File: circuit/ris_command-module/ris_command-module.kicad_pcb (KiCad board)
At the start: 2 copper layers, 48 x 71 mm, 7 parts, among them J1 JST-PH-5P-M, J3 JST-PH-2P-M, SW3 SW_DIP_x01, U1 AM2302_DHT22, U6 ESP32-DEVKITC-32D

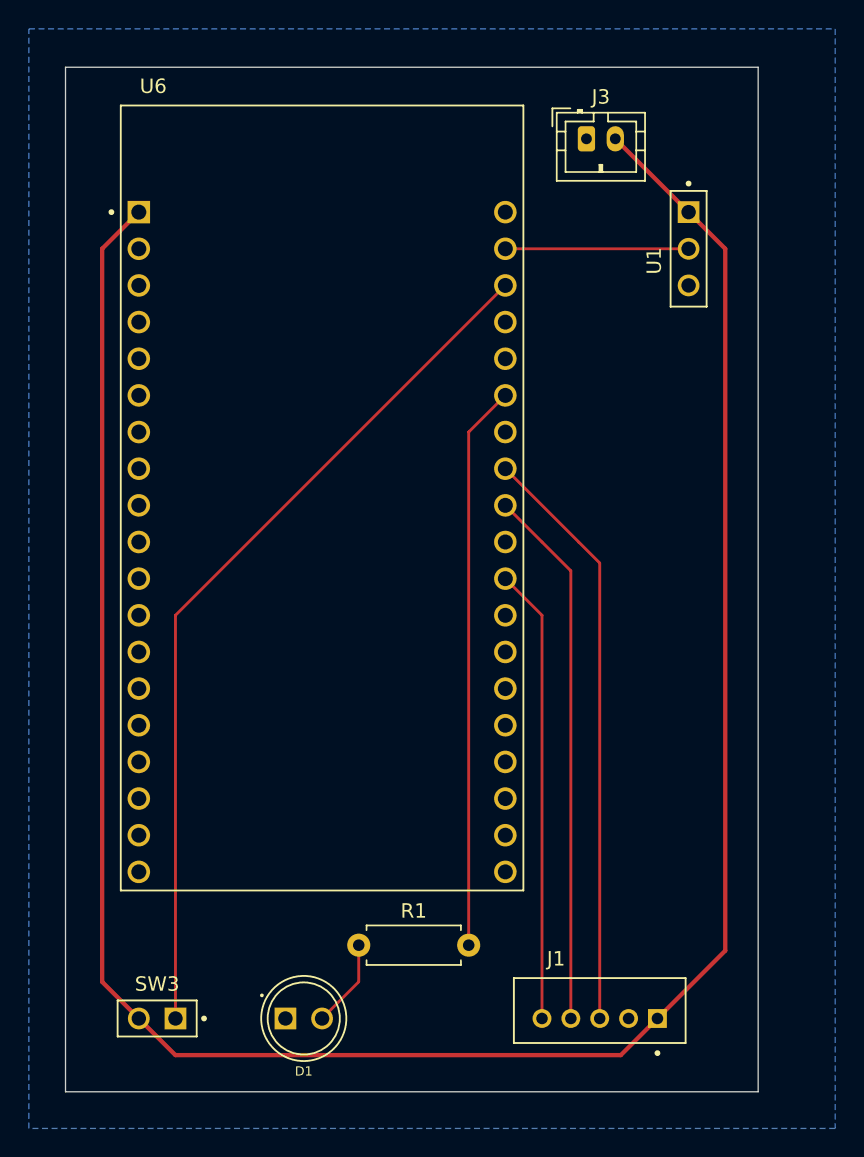
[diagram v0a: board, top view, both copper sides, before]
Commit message: Updated Circuit with Side Outputs & Mosfets
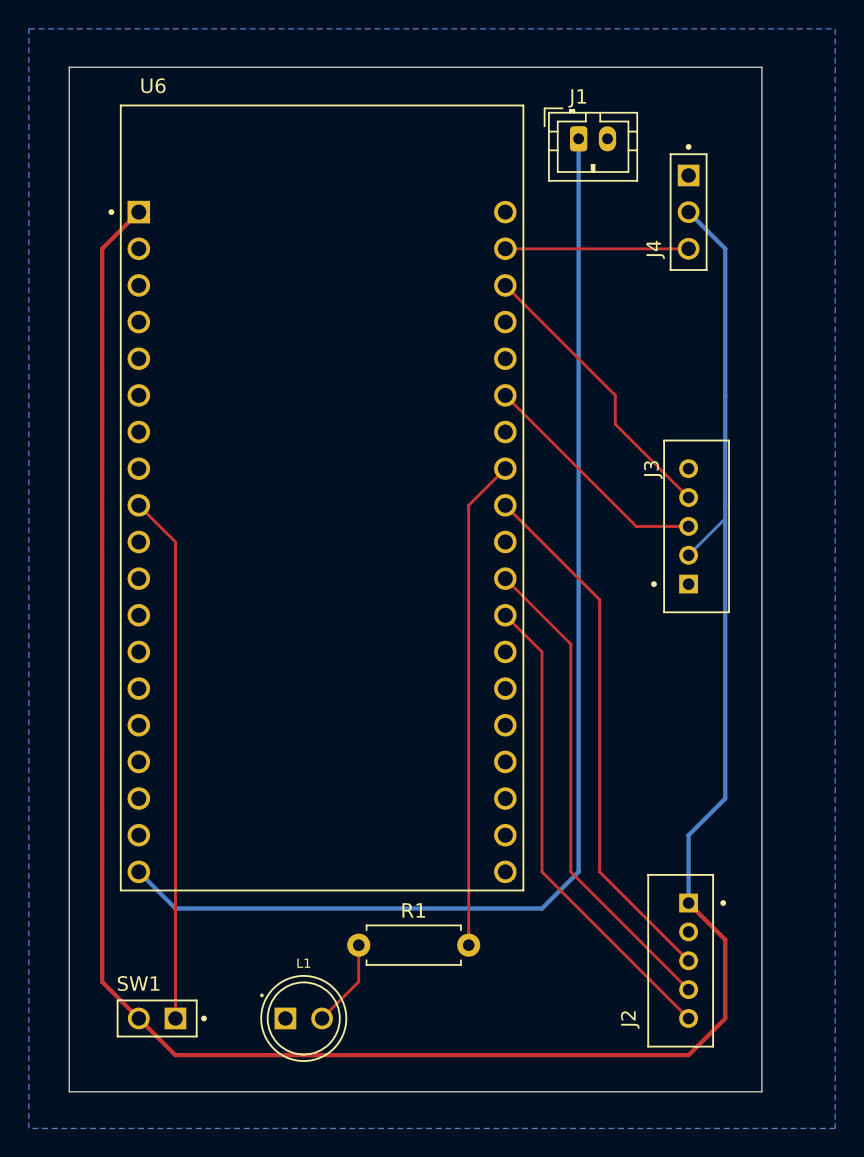
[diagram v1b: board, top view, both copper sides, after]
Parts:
- removed SW3: SW_DIP_x01, socket-headers-2pin:HARWIN_M20-7820242
- removed U1: AM2302_DHT22, socket-headers-3pin:HARWIN_M20-7820346
- added J1: JST-PH-2P-M_5V, Connector_JST:JST_PH_B2B-PH-K_1x02_P2.00mm_Vertical, F.Cu at (160.0, 68.6)
- added J4: Header-3P-F_DHT22, socket-headers-3pin:HARWIN_M20-7820346, F.Cu at (167.6, 73.7)
- added SW1: SW_DIP_x01, socket-headers-2pin:HARWIN_M20-7820242, F.Cu at (132.1, 129.5)
- J3: value JST-PH-2P-M -> JST-PH-5P-M_ZS042; footprint Connector_JST:JST_PH_B2B-PH-K_1x02_P2.00mm_Vertical -> B5B-PH-K-S:JST_B5B-PH-K-S
- moved J3 27.9 mm to (168.2, 95.4), turned to -90 degrees
- moved J2 6.59 mm to (167.1, 125.5), turned to 90 degrees
- renumbered J1 to J2, D1 to L1
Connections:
- J2 pad 3: Net-(J1-Pin_3) -> Net-(J2-Pin_3)
- J2 pad 4: Net-(J1-Pin_4) -> Net-(J2-Pin_4)
- J2 pad 5: Net-(J1-Pin_5) -> Net-(J2-Pin_5)
- R1 pad 2: Net-(U6-IO21) -> Net-(U6-IO19)
- U6 pad J2-19: unconnected-(U6-EXT_5V-PadJ2-19) -> +5V
- U6 pad J2-9: unconnected-(U6-IO25-PadJ2-9) -> Net-(U6-IO25)
- U6 pad J3-11: Net-(J1-Pin_5) -> Net-(J2-Pin_4)
- U6 pad J3-12: unconnected-(U6-IO16-PadJ3-12) -> Net-(J2-Pin_5)
- U6 pad J3-3: Net-(U6-IO22) -> Net-(J3-Pin_4)
- U6 pad J3-6: Net-(U6-IO21) -> Net-(J3-Pin_3)
- U6 pad J3-8: Net-(J1-Pin_3) -> Net-(U6-IO19)
- U6 pad J3-9: Net-(J1-Pin_4) -> Net-(J2-Pin_3)
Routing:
- net +5V: track 0.00 -> 83.4 mm
- net Net-(U6-IO22): track 60.3 -> 0.00 mm
- net Net-(J1-Pin_3): track 40.8 -> 0.00 mm
- net Net-(U6-IO21): track 39.2 -> 0.00 mm
- net Net-(J1-Pin_4): track 37.4 -> 0.00 mm
- net Net-(J2-Pin_3): track 0.00 -> 36.8 mm
- net Net-(U6-IO25): track 0.00 -> 36.6 mm
- net Net-(U6-IO19): track 0.00 -> 34.1 mm
- net Net-(J2-Pin_4): track 0.00 -> 33.7 mm
- net Net-(J2-Pin_5): track 0.00 -> 33.2 mm
- net Net-(J1-Pin_5): track 31.5 -> 0.00 mm
- net Net-(J3-Pin_4): track 0.00 -> 20.0 mm
- net Net-(J3-Pin_3): track 0.00 -> 16.8 mm
- net +3.3V: track 162.1 -> 164.3 mm

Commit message: Updated Model with Connectors / Slots
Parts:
- moved J2 4.70 mm to (167.1, 120.8)
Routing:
- net Net-(J2-Pin_3): track 36.8 -> 32.5 mm
- net Net-(J2-Pin_4): track 33.7 -> 29.4 mm
- net Net-(J2-Pin_5): track 33.2 -> 28.9 mm
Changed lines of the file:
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@@
 	(footprint "B5B-PH-K-S:JST_B5B-PH-K-S"
 		(layer "F.Cu")
-		(at 167.09 125.54 90)
+		(at 167.09 120.84 90)
 		(property "Reference" "J2"
 			(at -4 -3.585 90)
@@
 		(model "G:/projects/primary/regulated-irrigation-system/model/asm/electronic-components/jst-ph-5p_short/jst-ph-5p_short.step"
 			(offset
-				(xyz 4.55 -4.1 6)
+				(xyz 4 -0.55 6)
 			)
 			(scale
@@
 		(model "G:/projects/primary/regulated-irrigation-system/model/asm/electronic-components/led/led.step"
 			(offset
-				(xyz -0.8 -4.5 10.74)
+				(xyz -0.12 -5.68 9.68)
 			)
 			(scale
@@
 		(model "G:/projects/primary/regulated-irrigation-system/model/asm/electronic-components/switch/switch.step"
 			(offset
-				(xyz 5.3 -5.3 13.5)
+				(xyz 9.75 -16.8 18.07)
 			)
 			(scale
@@
 	)
 	(segment
+		(start 170.18 129.54)
+		(end 170.18 119.38)
+		(width 0.3)
+		(layer "F.Cu")
+		(net 3)
+	)
+	(segment
+		(start 129.54 73.66)
+		(end 127 76.2)
+		(width 0.3)
+		(layer "F.Cu")
+		(net 3)
+	)
+	(segment
 		(start 132.08 132.08)
 		(end 167.64 132.08)
@@
 	)
 	(segment
-		(start 129.54 73.66)
-		(end 127 76.2)
+		(start 129.54 129.54)
+		(end 132.08 132.08)
 		(width 0.3)
 		(layer "F.Cu")
@@
 	)
 	(segment
-		(start 170.18 129.54)
-		(end 170.18 124.08)
+		(start 170.18 119.38)
+		(end 167.64 116.84)
 		(width 0.3)
 		(layer "F.Cu")
@@
 	)
 	(segment
-		(start 170.18 124.08)
-		(end 167.64 121.54)
-		(width 0.3)
-		(layer "F.Cu")
-		(net 3)
-	)
-	(segment
 		(start 127 127)
 		(end 129.54 129.54)
-		(width 0.3)
-		(layer "F.Cu")
-		(net 3)
-	)
-	(segment
-		(start 129.54 129.54)
-		(end 132.08 132.08)
 		(width 0.3)
 		(layer "F.Cu")
@@
 	)
 	(segment
-		(start 167.64 121.54)
-		(end 167.64 116.84)
-		(width 0.3)
-		(layer "B.Cu")
-		(net 3)
-	)
-	(segment
 		(start 167.64 97.44)
 		(end 170.18 94.9)
@@
 	)
 	(segment
+		(start 167.02 120.84)
+		(end 161.48 115.3)
+		(width 0.2)
+		(layer "F.Cu")
+		(net 33)
+	)
+	(segment
+		(start 167.64 120.84)
+		(end 167.02 120.84)
+		(width 0.2)
+		(layer "F.Cu")
+		(net 33)
+	)
+	(segment
+		(start 161.48 115.3)
+		(end 161.48 100.52)
+		(width 0.2)
+		(layer "F.Cu")
+		(net 33)
+	)
+	(segment
 		(start 161.48 100.52)
 		(end 154.94 93.98)
@@
 	)
 	(segment
-		(start 167.64 125.54)
-		(end 161.48 119.38)
-		(width 0.2)
-		(layer "F.Cu")
-		(net 33)
-	)
-	(segment
-		(start 161.48 119.38)
-		(end 161.48 100.52)
-		(width 0.2)
-		(layer "F.Cu")
-		(net 33)
-	)
-	(segment
-		(start 167.64 129.54)
-		(end 157.48 119.38)
-		(width 0.2)
-		(layer "F.Cu")
-		(net 34)
-	)
-	(segment
-		(start 157.48 119.38)
-		(end 157.48 104.14)
+		(start 167.02 124.84)
+		(end 157.48 115.3)
 		(width 0.2)
 		(layer "F.Cu")
@@
 	)
 	(segment
-		(start 159.48 119.38)
+		(start 167.64 124.84)
+		(end 167.02 124.84)
+		(width 0.2)
+		(layer "F.Cu")
+		(net 34)
+	)
+	(segment
+		(start 157.48 115.3)
+		(end 157.48 104.14)
+		(width 0.2)
+		(layer "F.Cu")
+		(net 34)
+	)
+	(segment
+		(start 167.02 122.84)
+		(end 159.48 115.3)
+		(width 0.2)
+		(layer "F.Cu")
+		(net 35)
+	)
+	(segment
+		(start 159.48 115.3)
 		(end 159.48 103.6)
+		(width 0.2)
+		(layer "F.Cu")
+		(net 35)
+	)
+	(segment
+		(start 167.64 122.84)
+		(end 167.02 122.84)
 		(width 0.2)
 		(layer "F.Cu")
@@
 		(width 0.2)
 		(layer "F.Cu")
-		(net 35)
-	)
-	(segment
-		(start 167.64 127.54)
-		(end 159.48 119.38)
-		(width 0.2)
-		(layer "F.Cu")

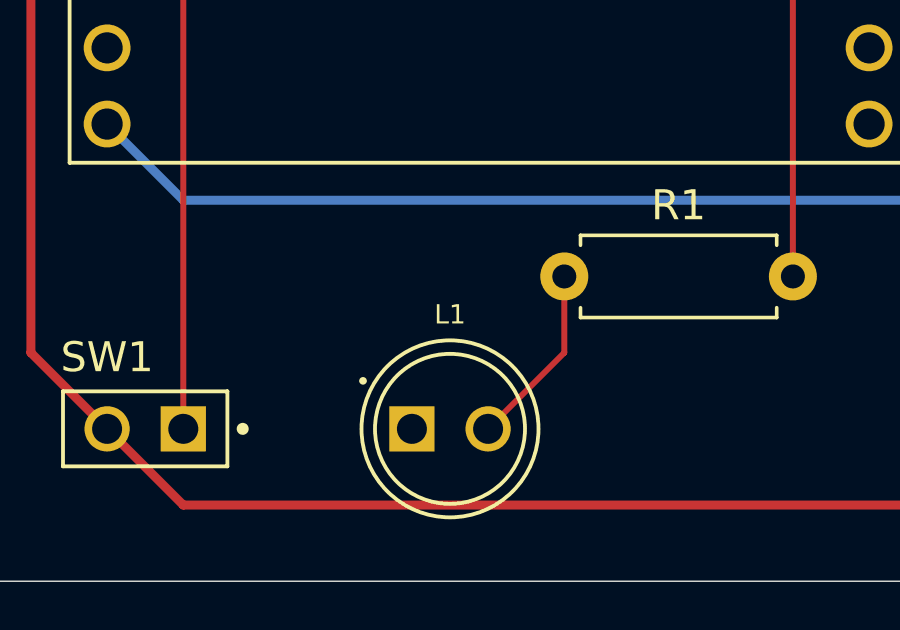
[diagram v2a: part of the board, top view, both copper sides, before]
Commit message: Fixed Circuit by DRC
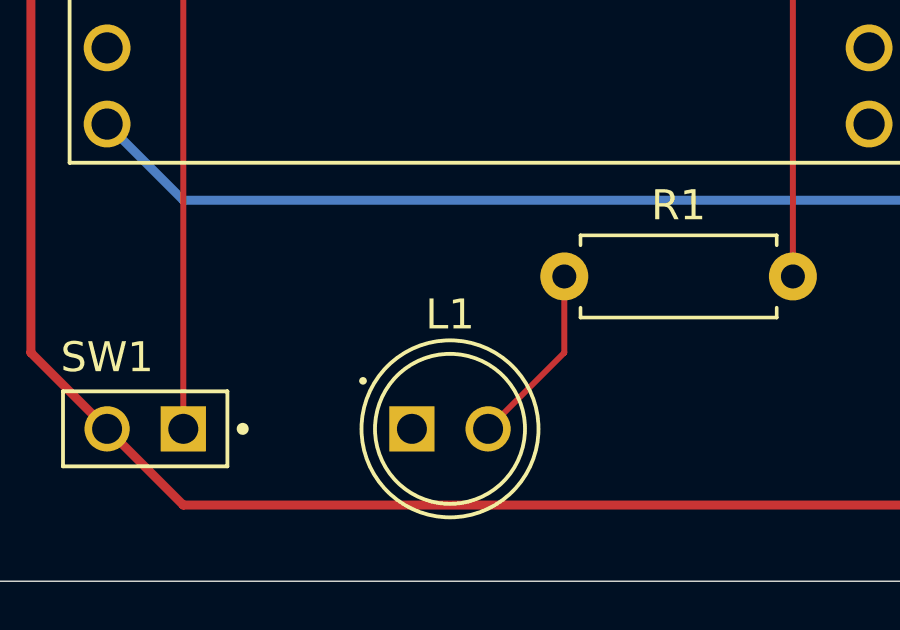
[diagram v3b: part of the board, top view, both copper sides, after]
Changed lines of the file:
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@@
 			(outputformat 1)
 			(mirror no)
-			(drillshape 1)
+			(drillshape 0)
 			(scaleselection 1)
-			(outputdirectory "")
+			(outputdirectory "gerber/")
 		)
 	)
@@
 			(effects
 				(font
-					(size 0.641222 0.641222)
-					(thickness 0.15)
-				)
+					(size 1 1)
+					(thickness 0.15)
+				)

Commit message: Exported Circuits to Gerber files
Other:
- board text added: "RIS - COMMAND MODULE v1.0.0 - SAM DIXON"
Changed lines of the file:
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@@
 			(drillshape 0)
 			(scaleselection 1)
-			(outputdirectory "gerber/")
+			(outputdirectory "ris_command-module_gerber/")
 		)
 	)
@@
 		(layer "Edge.Cuts")
 	)
+	(gr_text "RIS - COMMAND MODULE\nv1.0.0 - SAM DIXON"
+		(at 152.4 133.35 0)
+		(layer "F.SilkS")
+		(effects
+			(font
+				(size 1 1)
+				(thickness 0.15)
+			)
+			(justify left bottom)
+		)
+	)
 	(segment
